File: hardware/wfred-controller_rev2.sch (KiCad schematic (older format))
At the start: 10 parts, among them IC201 ATMEGA328P-A, P201 ISP, X201 myCRYSTAL

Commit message: Added Reichelt/Mouser part numbers for all parts except ESP12-E/F
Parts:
- C201, C202, C203, C204: Reichelt (none) -> X7R-G0805 100N
- C205, C206: Reichelt (none) -> NPO-G0805 22P
- IC201: Mouser (none) -> 556-ATMEGA328P-AU
- P201: Reichelt WSL 6W -> SL 2X10G SMD2,54 / SL 2X10G 2,54
- R201: Mouser (none) -> 603-RC0805JR-0710KL
- X201: Mouser (none) -> 449-LFXTAL036338CUTT
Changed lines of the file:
@@
 F 2 "Capacitors_SMD:C_0805_HandSoldering" H 7738 3450 30  0001 C CNN
 F 3 "" H 7700 3600 60  0000 C CNN
+F 4 "NPO-G0805 22P" H 7700 3600 60  0001 C CNN "Reichelt"
 	1    7700 3600
 	0    -1   1    0
@@
 F 2 "Capacitors_SMD:C_0805_HandSoldering" H 7738 4250 30  0001 C CNN
 F 3 "" H 7700 4400 60  0000 C CNN
+F 4 "NPO-G0805 22P" H 7700 4400 60  0001 C CNN "Reichelt"
 	1    7700 4400
 	0    -1   1    0
@@
 F 2 "Capacitors_SMD:C_0805_HandSoldering" H 4438 1950 30  0001 C CNN
 F 3 "" H 4400 2100 60  0000 C CNN
+F 4 "X7R-G0805 100N" H 4400 2100 60  0001 C CNN "Reichelt"
 	1    4400 2100
 	1    0    0    -1
@@
 F 2 "Capacitors_SMD:C_0805_HandSoldering" H 4738 1950 30  0001 C CNN
 F 3 "" H 4700 2100 60  0000 C CNN
+F 4 "X7R-G0805 100N" H 4700 2100 60  0001 C CNN "Reichelt"
 	1    4700 2100
 	1    0    0    -1
@@
 F 2 "Capacitors_SMD:C_0805_HandSoldering" H 5038 1950 30  0001 C CNN
 F 3 "" H 5000 2100 60  0000 C CNN
+F 4 "X7R-G0805 100N" H 5000 2100 60  0001 C CNN "Reichelt"
 	1    5000 2100
 	1    0    0    -1
@@
 F 2 "Capacitors_SMD:C_0805_HandSoldering" H 2138 4150 30  0001 C CNN
 F 3 "" H 2100 4300 60  0000 C CNN
+F 4 "X7R-G0805 100N" H 2100 4300 60  0001 C CNN "Reichelt"
 	1    2100 4300
 	1    0    0    -1
@@
 F 2 "Pin_Headers:Pin_Header_Straight_2x03_Pitch2.54mm" H 3500 2250 60  0001 C CNN
 F 3 "" H 3500 2250 60  0001 C CNN
-F 4 "WSL 6W" H 3500 2250 60  0001 C CNN "Reichelt"
+F 4 "SL 2X10G SMD2,54 / SL 2X10G 2,54" H 3500 2250 60  0001 C CNN "Reichelt"
 	1    3500 2250
 	1    0    0    -1
@@
 F 2 "Capacitors_SMD:C_0805_HandSoldering" V 3480 1700 30  0001 C CNN
 F 3 "" H 3550 1700 30  0000 C CNN
+F 4 "603-RC0805JR-0710KL" V 3550 1700 60  0001 C CNN "Mouser"
 	1    3550 1700
 	0    1    1    0
@@
 F 2 "Housings_QFP:TQFP-32_7x7mm_Pitch0.8mm" H 3900 4400 30  0000 C CIN
 F 3 "" H 3900 4400 60  0001 C CNN
+F 4 "556-ATMEGA328P-AU" H 3900 4400 60  0001 C CNN "Mouser"
 	1    3900 4400
 	1    0    0    -1
@@
 F 2 "Crystals:Crystal_SMD_TXC_7M-4pin_3.2x2.5mm_HandSoldering" H 7200 4000 60  0001 C CNN
 F 3 "" H 7200 4000 60  0000 C CNN
+F 4 "449-LFXTAL036338CUTT" H 7200 4000 60  0001 C CNN "Mouser"
 	1    7200 4000
 	0    1    1    0

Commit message: Created new 3D renderings
- In the process, kicad "rescued" some symbols
- Also added the value to the crystal in the schematic
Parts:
- C201, C202, C203, C204, C205, C206: symbol C -> C-RESCUE-wfred_rev2
- R201: symbol R -> R-RESCUE-wfred_rev2
- X201: value myCRYSTAL -> 14.7456MHz
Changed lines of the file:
@@
 EESchema Schematic File Version 2
+LIBS:wfred_rev2-rescue
 LIBS:power
 LIBS:device
@@
 LIBS:my_devices
 LIBS:ESP8266
-LIBS:wfred_loconet_clock-cache
+LIBS:wfred_rev2-cache
 EELAYER 25 0
 EELAYER END
 $Descr A4 11693 8268
 encoding utf-8
-Sheet 2 5
+Sheet 2 4
 Title "Wireless FREDI (and clock interface)"
 Date "2017-11-19"
@@
 $EndDescr
 $Comp
-L C C205
+L C-RESCUE-wfred_rev2 C205
 U 1 1 5920CFB6
 P 7700 3600
+AR Path="/5920CFB6" Ref="C205"  Part="1"
+AR Path="/5920C945/5920CFB6" Ref="C205"  Part="1"
 F 0 "C205" H 7700 3700 40  0000 L CNN
 F 1 "22p" H 7706 3515 40  0000 L CNN
@@
 $EndComp
 $Comp
-L C C206
+L C-RESCUE-wfred_rev2 C206
 U 1 1 5920D023
 P 7700 4400
+AR Path="/5920D023" Ref="C206"  Part="1"
+AR Path="/5920C945/5920D023" Ref="C206"  Part="1"
 F 0 "C206" H 7700 4500 40  0000 L CNN
 F 1 "22p" H 7706 4315 40  0000 L CNN
@@
 $EndComp
 $Comp
-L C C202
+L C-RESCUE-wfred_rev2 C202
 U 1 1 5920D0A7
 P 4400 2100
+AR Path="/5920D0A7" Ref="C202"  Part="1"
+AR Path="/5920C945/5920D0A7" Ref="C202"  Part="1"
 F 0 "C202" H 4400 2200 40  0000 L CNN
 F 1 "100n" H 4406 2015 40  0000 L CNN
@@
 $EndComp
 $Comp
-L C C203
+L C-RESCUE-wfred_rev2 C203
 U 1 1 5920E33B
 P 4700 2100
+AR Path="/5920E33B" Ref="C203"  Part="1"
+AR Path="/5920C945/5920E33B" Ref="C203"  Part="1"
 F 0 "C203" H 4700 2200 40  0000 L CNN
 F 1 "100n" H 4706 2015 40  0000 L CNN
@@
 $EndComp
 $Comp
-L C C204
+L C-RESCUE-wfred_rev2 C204
 U 1 1 5920E379
 P 5000 2100
+AR Path="/5920E379" Ref="C204"  Part="1"
+AR Path="/5920C945/5920E379" Ref="C204"  Part="1"
 F 0 "C204" H 5000 2200 40  0000 L CNN
 F 1 "100n" H 5006 2015 40  0000 L CNN
@@
 $EndComp
 $Comp
-L C C201
+L C-RESCUE-wfred_rev2 C201
 U 1 1 5920E47C
 P 2100 4300
+AR Path="/5920E47C" Ref="C201"  Part="1"
+AR Path="/5920C945/5920E47C" Ref="C201"  Part="1"
 F 0 "C201" H 2100 4400 40  0000 L CNN
 F 1 "100n" H 2106 4215 40  0000 L CNN
@@
 $EndComp
 $Comp
-L R R201
+L R-RESCUE-wfred_rev2 R201
 U 1 1 5920FD60
 P 3550 1700
@@
 $EndComp
 $Comp
-L GND #PWR014
+L GND-RESCUE-wfred_rev2 #PWR014
 U 1 1 5920D54C
 P 8100 4600
@@
 $EndComp
 $Comp
-L GND #PWR015
+L GND-RESCUE-wfred_rev2 #PWR015
 U 1 1 5920D60E
 P 4400 2700
@@
 Connection ~ 2700 3400
 $Comp
-L GND #PWR019
+L GND-RESCUE-wfred_rev2 #PWR019
 U 1 1 592F4690
 P 2100 4700
@@
 $EndComp
 $Comp
-L GND #PWR020
+L GND-RESCUE-wfred_rev2 #PWR020
 U 1 1 592F46BC
 P 2700 5900
@@
 P 7200 4000
 F 0 "X201" H 7200 4150 60  0000 C CNN
-F 1 "myCRYSTAL" H 7200 3850 60  0000 C CNN
+F 1 "14.7456MHz" H 7200 3850 60  0000 C CNN
 F 2 "Crystals:Crystal_SMD_TXC_7M-4pin_3.2x2.5mm_HandSoldering" H 7200 4000 60  0001 C CNN
 F 3 "" H 7200 4000 60  0000 C CNN
@@
 $EndComp
 $Comp
-L GND #PWR021
+L GND-RESCUE-wfred_rev2 #PWR021
 U 1 1 5A171EC6
 P 7000 4600
@@
 $EndComp
 $Comp
-L GND #PWR022
+L GND-RESCUE-wfred_rev2 #PWR022
 U 1 1 5A171EEF
 P 6800 3800

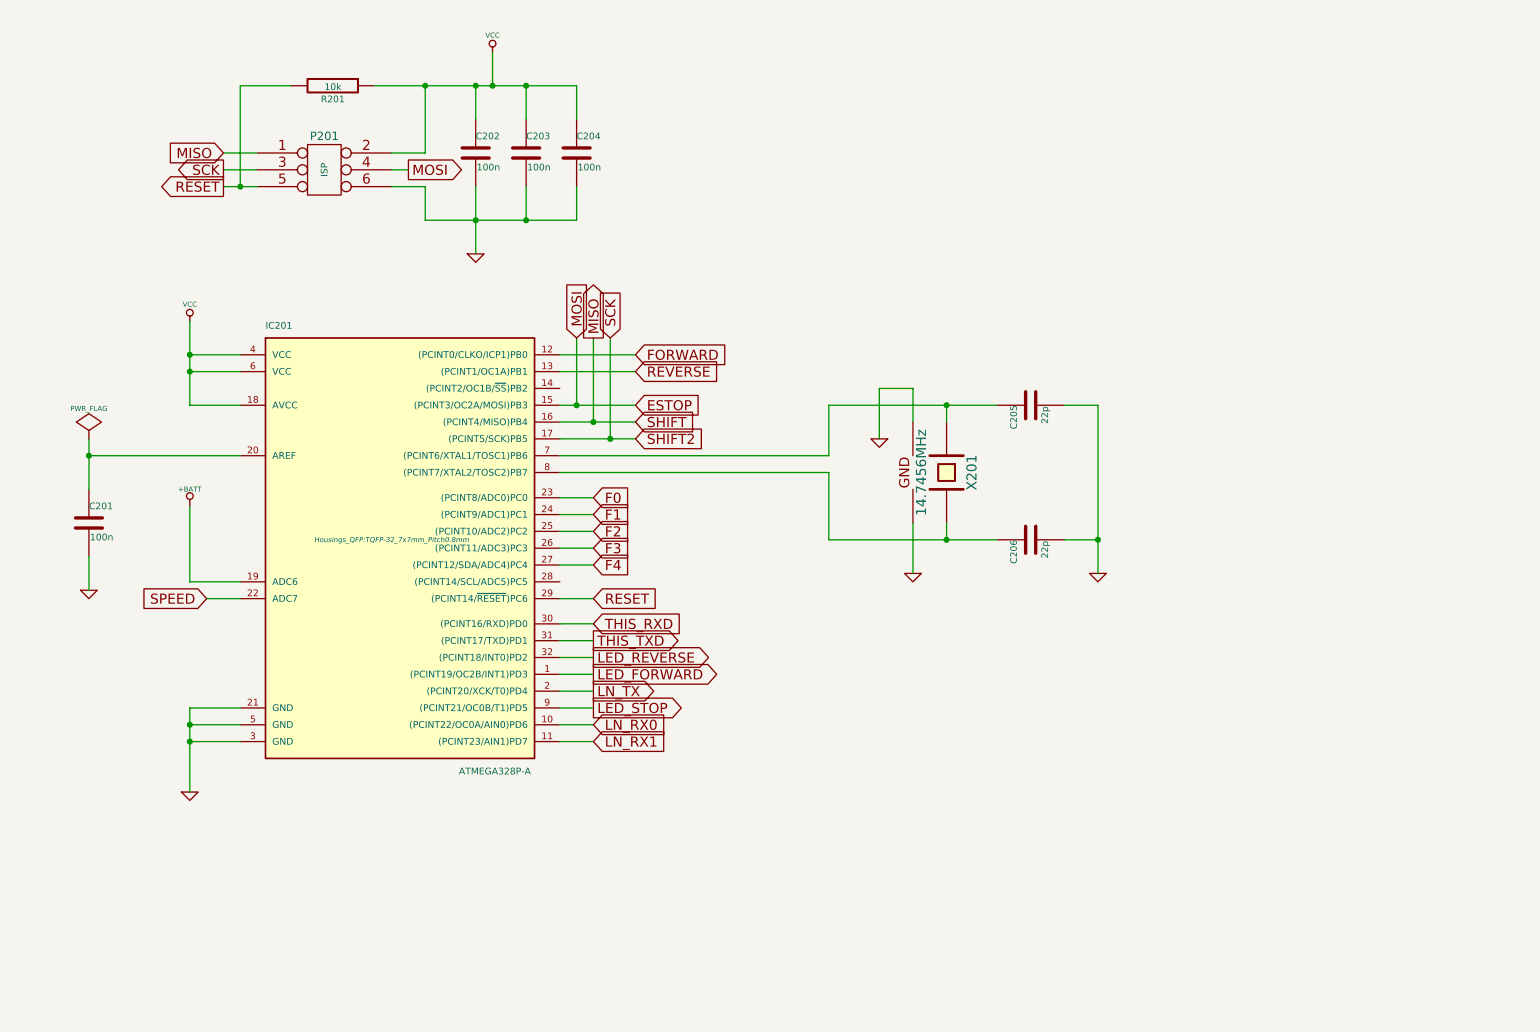
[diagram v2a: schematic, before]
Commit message: Switched schematic over to LiPo cell
- Removed AA battery holder
- Removed switching power regulator
- Added micro USB connector
- Added two pin battery connector
- Added LiPo charging IC
- Added 3.0V linear regulator
- Replaced ATMega328 with ATMega32
- Added F5-F8 keys
- Removed SHIFT2 key
- Moved LOCO keys from ESP to ATMega32
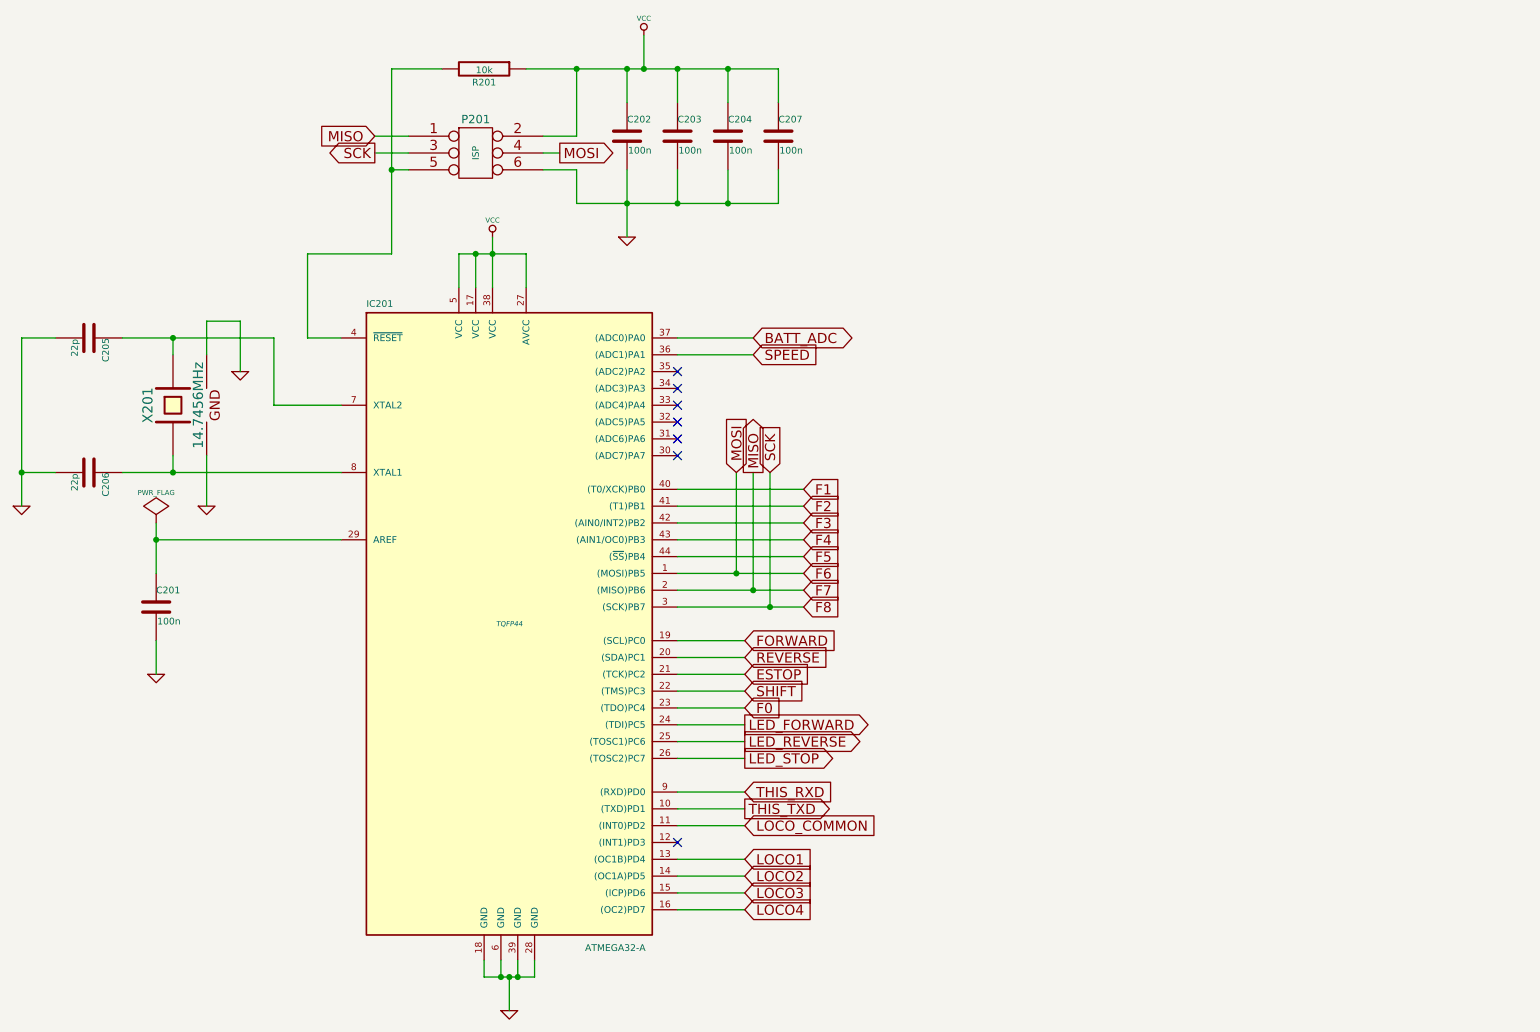
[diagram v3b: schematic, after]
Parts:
- removed IC201: ATMEGA328P-A, Housings_QFP:TQFP-32_7x7mm_Pitch0.8mm, symbol ATMEGA328P-A
- added C207: 100n, Capacitors_SMD:C_0805_HandSoldering, symbol C-RESCUE-wfred_rev2
- added IC201: ATMEGA32-A, TQFP44, symbol ATMEGA32-A
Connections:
- net ESTOP: now also IC201.21 ((TCK)PC2); no longer P201.4
- net F0: now also IC201.23 ((TDO)PC4)
- net F1: now also IC201.40 ((T0/XCK)PB0)
- net F2: now also IC201.41 ((T1)PB1)
- net F3: now also IC201.42 ((AIN0/INT2)PB2)
- net F4: now also IC201.43 ((AIN1/OC0)PB3)
- net FORWARD: now also IC201.19 ((SCL)PC0)
- net GND: now also C207.2, IC201.18 (GND), IC201.28 (GND), IC201.39 (GND), IC201.6 (GND)
- net LED_FORWARD: now also IC201.24 ((TDI)PC5)
- net LED_REVERSE: now also IC201.25 ((TOSC1)PC6)
- net LED_STOP: now also IC201.26 ((TOSC2)PC7)
- net REVERSE: now also IC201.20 ((SDA)PC1)
- net SPEED: now also IC201.36 ((ADC1)PA1)
- net THIS_RXD: now also IC201.9 ((RXD)PD0)
- net THIS_TXD: now also IC201.10 ((TXD)PD1)
- net VCC: now also C207.1, IC201.17 (VCC), IC201.27 (AVCC), IC201.38 (VCC), IC201.5 (VCC)
- net at C205.1, X201.1: now also IC201.7 (XTAL2)
- net at C206.1, X201.3: now also IC201.8 (XTAL1)
- net at C201.1: now also IC201.29 (AREF)
- net MISO renamed F7
- net F7: now also IC201.2 ((MISO)PB6)
- net RESET: no longer names the net of P201.5, R201.2
- net RESET: now also IC201.4 (~RESET)
- net SCK renamed F8
- net F8: now also IC201.3 ((SCK)PB7)
- new net BATT_ADC: IC201.37 ((ADC0)PA0)
- new net F5: IC201.44 ((~SS~)PB4)
- new net F6: IC201.1 ((MOSI)PB5), P201.4
- new net LOCO1: IC201.13 ((OC1B)PD4)
- new net LOCO2: IC201.14 ((OC1A)PD5)
- new net LOCO3: IC201.15 ((ICP)PD6)
- new net LOCO4: IC201.16 ((OC2)PD7)
- new net LOCO_COMMON: IC201.11 ((INT0)PD2)
- new net SHIFT: IC201.22 ((TMS)PC3)
- no-connect marks 0 -> 7
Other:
- moved on the sheet: C201, C202, C203, C204, C205, C206, P201, R201, X201

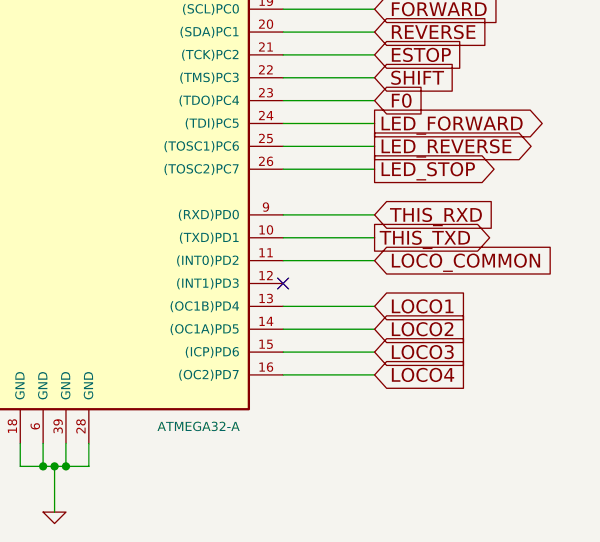
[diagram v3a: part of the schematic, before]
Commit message: Added ESP reset connection to AVR
- Enables ESP to go into deep sleep and be woken up by AVR
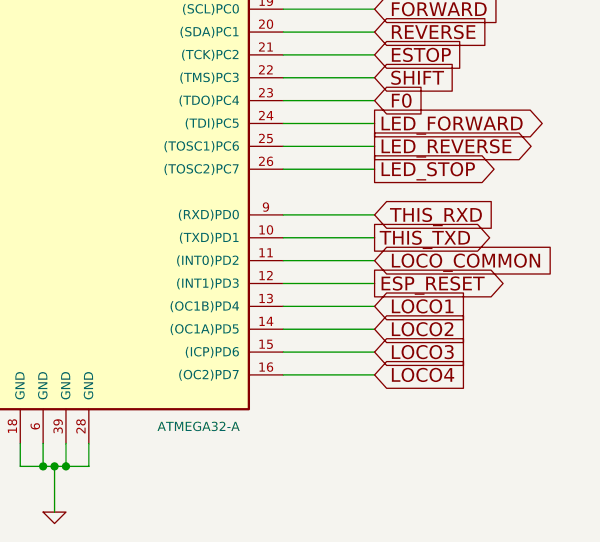
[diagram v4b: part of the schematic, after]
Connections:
- net ESP_RESET: now reaches IC201.12 ((INT1)PD3)
- no-connect marks 7 -> 6
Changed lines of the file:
@@
 Wire Wire Line
 	5600 5600 6000 5600
-NoConn ~ 5600 6200
 NoConn ~ 5600 3400
 NoConn ~ 5600 3500
@@
 Wire Wire Line
 	3900 2200 4000 2200
+Text GLabel 6000 6200 2    60   Output ~ 0
+ESP_RESET
+Wire Wire Line
+	5600 6200 6000 6200
 $EndSCHEMATC
